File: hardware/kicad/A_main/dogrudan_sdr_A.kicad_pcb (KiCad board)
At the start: 6 copper layers, 235 x 225 mm, 297 parts, among them J1 XT60, J10 JTAG 2x3, J20 SMA A1, J21 SMA B1, J22 SMA A2, J23 SMA B2, J30 SMA TX1, J31 SMA TX2, J32 SMA TX3, J33 SMA TX4, J40 HR911130A, J41 HR911130A, J60 GPS modul, J61 SMA 10MHz ref, J62 DAC modul, J63 C kartina, J64 UART 3.3V, J65 C kartina #2, J66 D kartina, Q1 DMP3098L, SW1 PROG, T1 ADT1-1WT+, T10 ADT1-1WT+, T11 ADT1-1WT+, T12 ADT1-1WT+, T13 ADT1-1WT+, T2 ADT1-1WT+, T3 ADT1-1WT+, T4 ADT1-1WT+, U1 TPS62130, U10 LFE5U-25F-7BG256I, U11 W25Q128JVSIQ, U15 ADCLK846BCPZ, U16 SN65LVDS2DBVR, U17 SN65LVDS2DBVR, U18 SN65LVDS2DBVR, U2 TPS62130, U20 AD9251BCPZ-80, U21 AD9251BCPZ-80, U3 TPS7A2033, U30 AD9767ASTZ, U31 AD9767ASTZ, U4 ADP150, U40 RTL8211FI-CG, U41 RTL8211FI-CG, U5 ADP150, U50 W9825G6KH-6I, U6 ADP150, U62 TLV3501AIDBVR, U7 ADP150, U8 ADP150, U9 ADP150, Y10 ABLNO-V-80.000MHZ, Y610 25MHz CL12pF, Y626 25MHz CL12pF

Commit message: Replace the transmit filters: harmonic suppression was illegal
Simulation of the output filters shows second-harmonic suppression
between 3 and 30 dB, where 43 dB is necessary below 30 MHz and 60 dB
above. On the 80/60 m position the second harmonic of 3.5 MHz is
3.4 dB down: the filter barely touches it. The transmitter would have
been out of specification on every band, and the board gives no sign
of it. Output power, SWR and efficiency all read correctly while the
harmonic radiates.

The cause is the band grouping. One position must pass 5.37 MHz, so
its cutoff is at 6.0, and the second harmonic of the same position's
lowest band, 3.5 MHz, falls at 7.0. More poles do not help: by the
Chebyshev attenuation formula, nine poles give 32 dB there.

Each series inductor now has a parallel capacitor that places a
transmission zero on the harmonic. 80 m and 60 m are separate
positions, because a trap at 7.0 MHz also attenuates a 5.37 MHz
passband. That uses the seventh relay, which was a bypass; a
transmitter with no harmonic filter in line is not legal in any case.

  band      loss   2nd harmonic   was
  160m      0.61   -82.4          -25.2
  80m       0.64   -80.7          grouped
  60m       0.45   -81.9          grouped
  40_30m    1.45   -58.0          -9.5
  20_17m    0.88   -68.4          -18.2
  15_10m    1.35   -61.0          -14.1
  6m        1.14   -82.8          -30.2
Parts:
- moved TP6 146.8 mm to (25.6, 50.4)
- moved TP10 83.6 mm to (125.8, 109.3)
- moved TP5 71.7 mm to (182.7, 199.3)
- moved TP7 68.1 mm to (140.5, 118.9)
- moved TP2 60.8 mm to (78.0, 129.9)
- moved TP3 50.7 mm to (72.1, 190.6)
- moved TP9 15.7 mm to (132.0, 132.8)
- moved C13 8.53 mm to (158.6, 173.3)
- moved TP1 8.17 mm to (22.0, 78.3)
- moved C502 5.87 mm to (147.1, 175.9)
- moved TP4 4.98 mm to (152.9, 170.2)

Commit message: Fit the filter bank and clear the overlaps
Board D's filter bank needs 285.6 mm of width with both inductors of
each band side by side, against about 236 mm available. Stacking them
vertically corrects the width and breaks the height: the strip
between the driver transformer and the relay row is 15.8 mm and a
stacked pair of T68 cores needs 37.7 mm.

Mapping the board in 10 mm bands gave the answer. Everything below
the relay row is the coupler and detector block at x above 250, while
the filter columns run from x 4 to 236. The space under them was
empty. The relay row moves from y 130 to 142 and its drivers from 155
to 172, with the filter block following. No board grew and the chain
stays in one row.

The separator never moves a part whose reference begins with U, J, T,
Y, L, Q, K or H, so two such parts overlapping cannot be separated
and the fix belongs in the placement rules. On A the XT60's courtyard
is 22.4 mm tall and snapped to the top edge, so it covered the
reverse-polarity MOSFET; the crystals and their inductors were placed
by the fallback and landed inside the PHY. All three now have
explicit positions.

The separator also gained a last resort: a movable part wedged so
that every push lands it in another part is relocated to the nearest
free position.

All three boards are at zero overlaps.
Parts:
- moved TP6 217.3 mm to (165.0, 217.1)
- moved TP5 108.7 mm to (107.8, 120.6)
- moved TP10 83.6 mm to (44.6, 89.6)
- moved TP7 68.1 mm to (80.1, 150.5)
- moved TP3 59.6 mm to (72.6, 131.0)
- moved C423 18.5 mm to (74.8, 134.1)
- moved C424 17.8 mm to (74.0, 194.2)
- moved C411 14.3 mm to (73.8, 126.2)
- moved C412 14.2 mm to (73.7, 185.9)
- moved TP2 12.7 mm to (67.7, 122.5)
- moved C407 11.4 mm to (62.8, 123.2)
- moved C13 8.53 mm to (159.3, 181.8)
- moved TP1 8.20 mm to (29.1, 74.3)
- moved C408 7.64 mm to (72.0, 189.8)
- moved C502 5.87 mm to (150.0, 170.8)
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
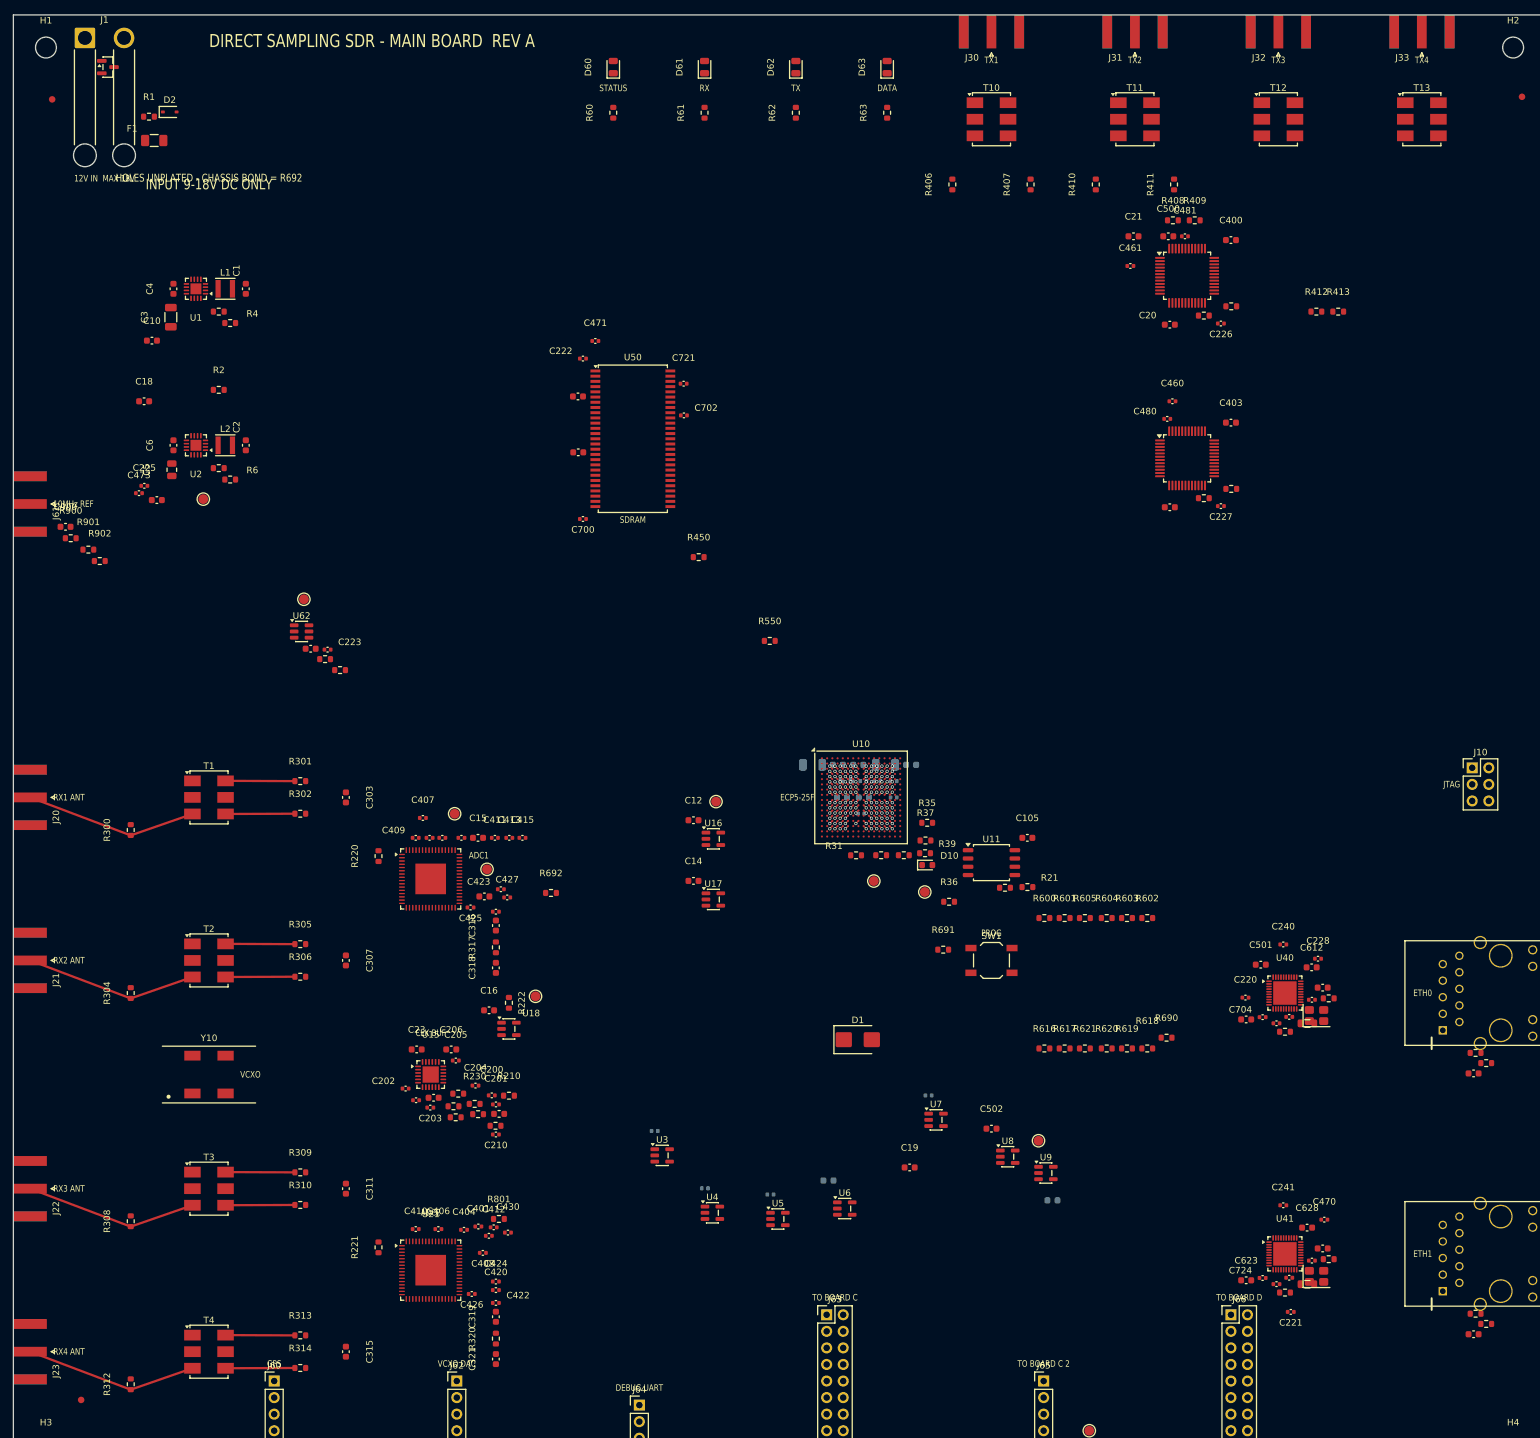
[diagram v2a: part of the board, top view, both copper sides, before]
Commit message: Close the last overlaps and record the pass that undid the other
Board D reaches zero overlaps. Two remained after the relay row
moved: a T68 clipping the driver transformer by 1 x 2 mm, and two
2N7002 transistors two millimetres apart, which the separator was
never going to touch because both begin with Q.

One finding is left on D. Tracing a single capacitor through every
stage shows the mechanism:

  pcb_kur          121.2 mm from the chip
  placement          5.1 mm   correct
  separation        21.0 mm   pushed away
  decoupling pass   25.3 mm   handed to another chip

The placer puts the capacitor beside the pin that needs it, the
separator finds an overlap and moves it, and the decoupling pass then
reads it as the nearest free capacitor for somebody else. The chip
that began with a correct capacitor ends with none.

The two steps disagreed about what an overlap is: the pass used a
1.4 mm margin while the separator used its courtyard box. What one
called clear the other called a collision. The pass now uses the
separator's measure. Its guard against taking a chip's only capacitor
was also too broad, counting chips connected through a logic input
tied high; it now applies the same power_in test.

What remains is to decide which of the two passes owns the final
position.
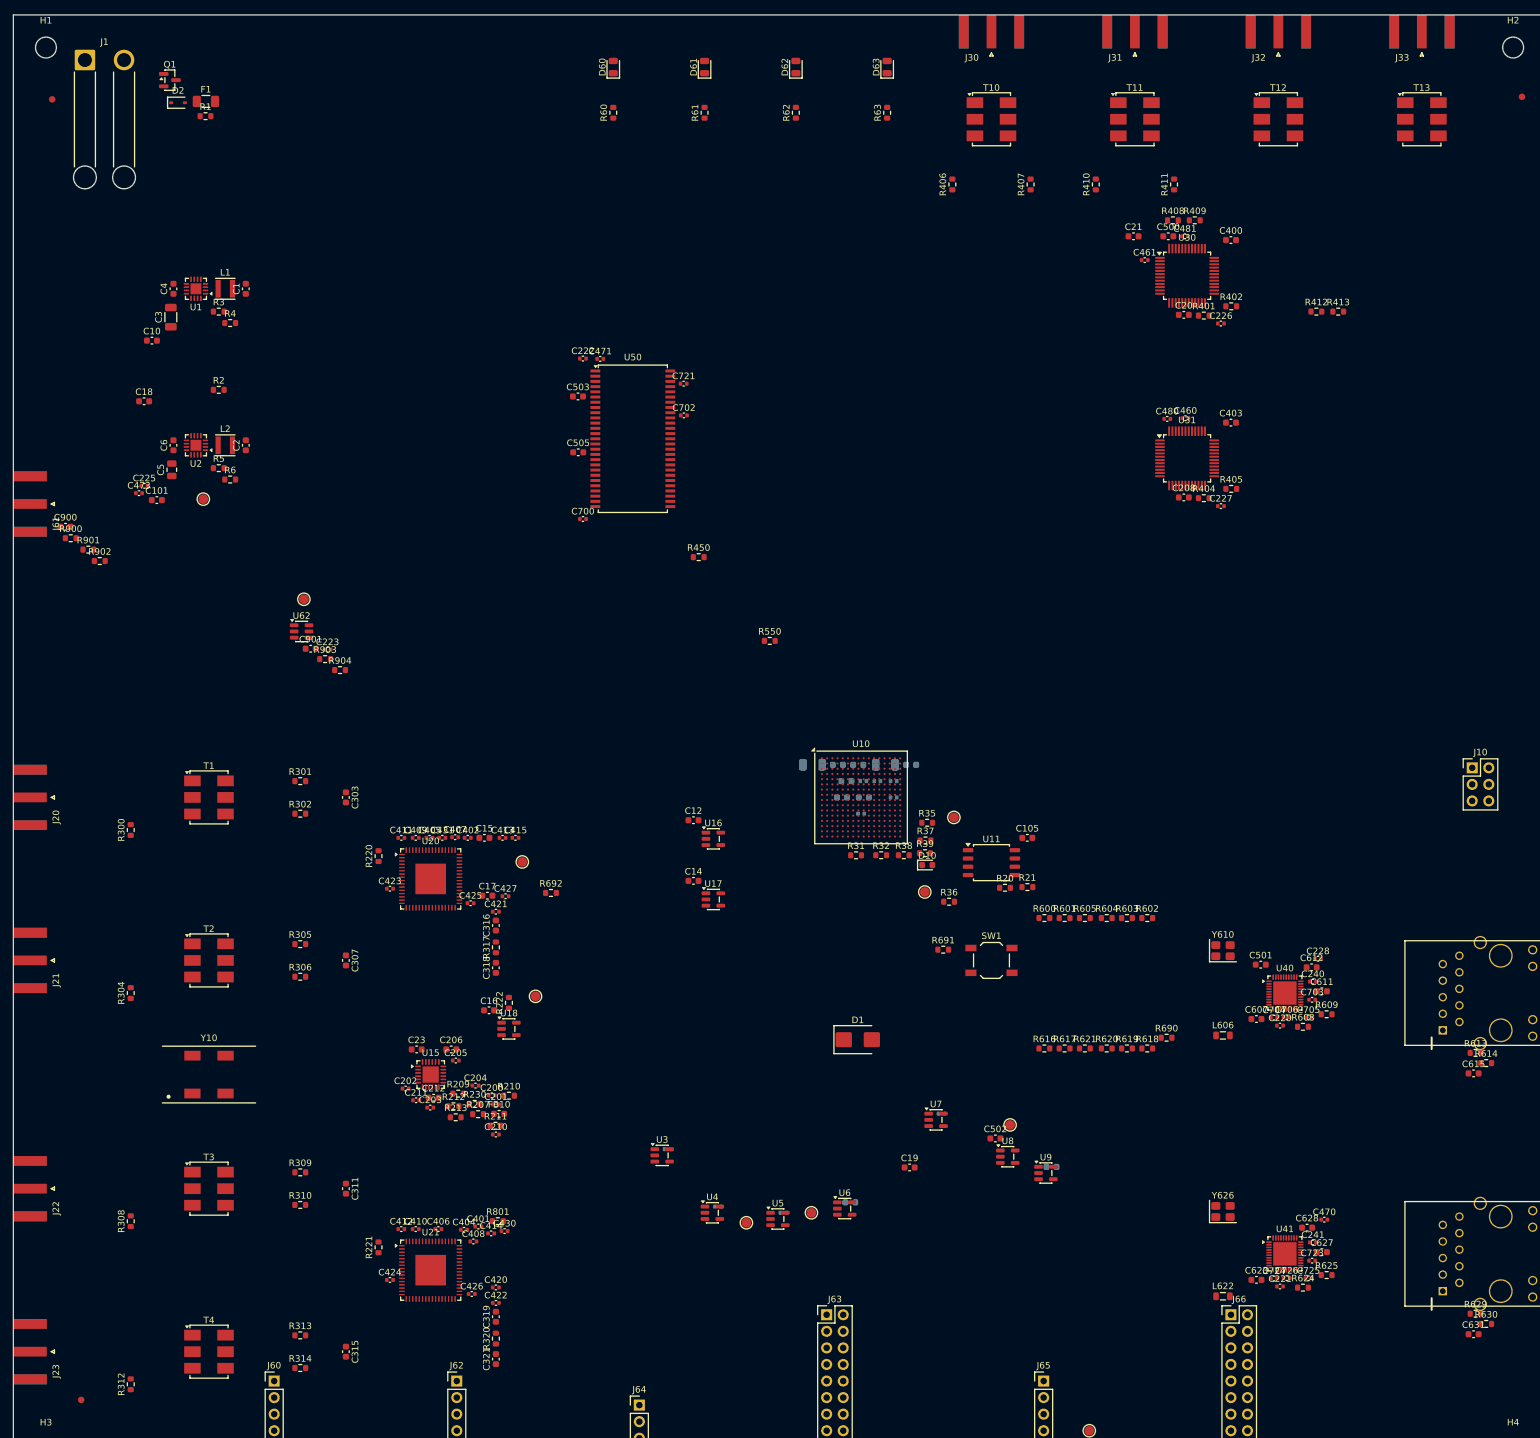
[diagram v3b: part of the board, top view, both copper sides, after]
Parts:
- moved TP3 72.5 mm to (122.4, 183.7)
- moved TP5 64.8 mm to (112.4, 185.2)
- moved Y610 17.5 mm to (185.5, 143.5)
- moved Y626 17.5 mm to (185.5, 183.5)
- moved C423 17.0 mm to (57.8, 134.0)
- moved C424 16.3 mm to (57.8, 194.0)
- moved TP9 15.7 mm to (144.2, 123.1)
- moved C411 14.3 mm to (59.5, 126.2)
- moved C412 14.2 mm to (59.5, 186.2)
- moved L606 13.1 mm to (185.5, 156.5)
- moved L622 13.1 mm to (185.5, 196.5)
- moved TP2 12.7 mm to (78.0, 129.9)
- moved F1 9.94 mm to (29.5, 13.3)
- moved Q1 9.71 mm to (24.0, 10.0)
- moved R1 8.67 mm to (29.5, 15.5)
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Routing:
- net RF_A1: track 26.5 -> 0.00 mm
- net RF_B2: track 26.5 -> 0.00 mm
- net RF_B1: track 26.5 -> 0.00 mm
- net RF_A2: track 26.5 -> 0.00 mm
- net SEC_B2_P: track 10.6 -> 0.00 mm
- net SEC_B2_N: track 10.6 -> 0.00 mm
- net SEC_B1_P: track 10.6 -> 0.00 mm
- net SEC_B1_N: track 10.6 -> 0.00 mm
- net SEC_A2_P: track 10.6 -> 0.00 mm
- net SEC_A2_N: track 10.6 -> 0.00 mm
- net SEC_A1_P: track 10.6 -> 0.00 mm
- net SEC_A1_N: track 10.6 -> 0.00 mm
- net GND: track 8.49 -> 0.00 mm, vias 15 -> 0
- net +3V3: track 5.09 -> 0.00 mm, vias 9 -> 0
- net +1V1: track 3.39 -> 0.00 mm, vias 6 -> 0
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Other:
- board text removed: "​10MHz REF"
- board text removed: "​12V IN MAX 18V"
- board text removed: "​ADC1"
- board text removed: "​ADC2"
- board text removed: "​CLK BUF"
- board text removed: "​DATA"
- board text removed: "​DEBUG UART"
- board text removed: "​DIRECT SAMPLING SDR - MAIN BOARD REV A"
- board text removed: "​ECP5-25F"
- board text removed: "​ETH0"
- board text removed: "​ETH1"
- board text removed: "​GPS"
- board text removed: "​HOLES UNPLATED - CHASSIS BOND = R692"
- board text removed: "​INPUT 9-18V DC ONLY"
- board text removed: "​JTAG"
- board text removed: "​PROG"
- board text removed: "​RX"
- board text removed: "​RX1 ANT"
- board text removed: "​RX2 ANT"
- board text removed: "​RX3 ANT"
- board text removed: "​RX4 ANT"
- board text removed: "​SDRAM"
- board text removed: "​STATUS"
- board text removed: "​TO BOARD C"
- board text removed: "​TO BOARD C 2"
- board text removed: "​TO BOARD D"
- board text removed: "​TX"
- board text removed: "​TX1"
- board text removed: "​TX2"
- board text removed: "​TX3"
- board text removed: "​TX4"
- board text removed: "​VCXO"
- board text removed: "​VCXO DAC"
